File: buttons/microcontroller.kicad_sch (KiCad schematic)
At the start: 32 parts, among them J2 USB_C_Receptacle_USB2.0, J3 Conn_01x03, SW17 SW_SPST, SW18 SW_SPST, U2 RP2040, U3 ip4234cz6, U4 AMS1117-3.3, Y1 12MHz

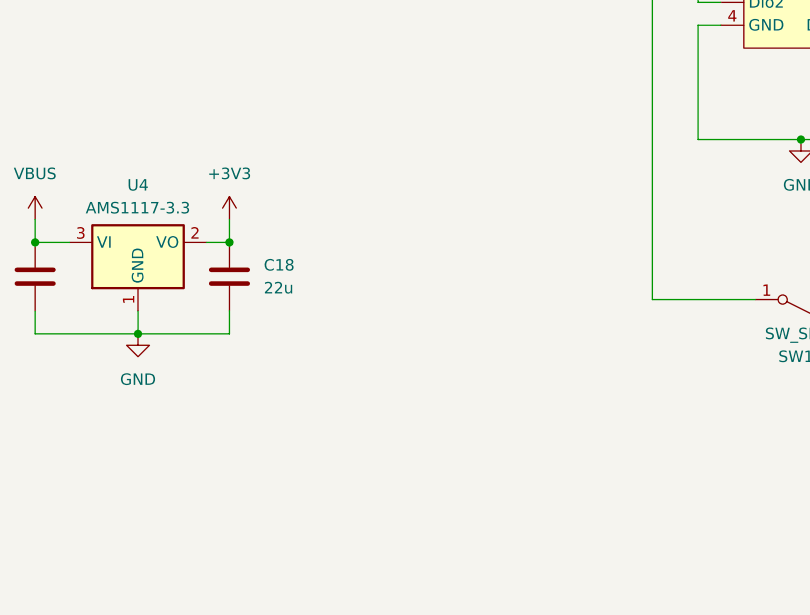
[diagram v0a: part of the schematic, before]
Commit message: Added power LED
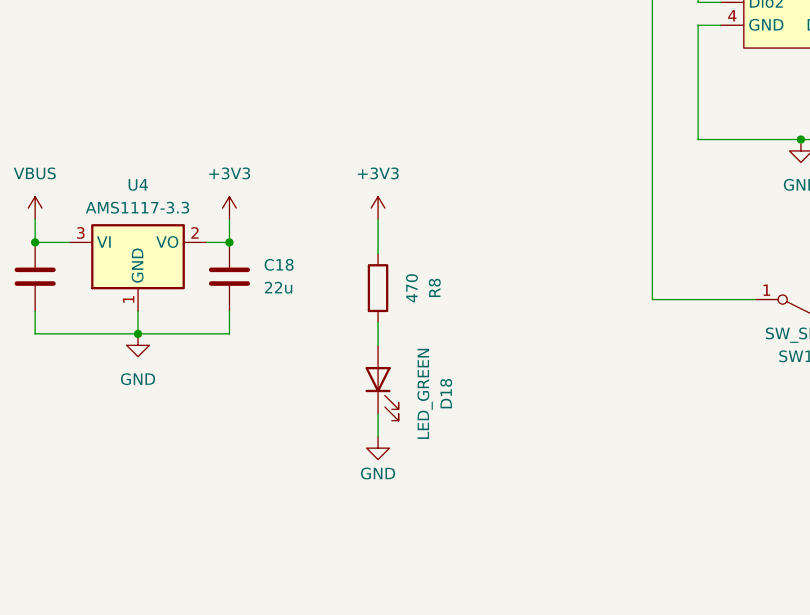
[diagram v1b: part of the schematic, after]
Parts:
- added D18: LED_GREEN, LED_SMD:LED_0603_1608Metric, symbol Device:LED
- added R8: 470, Resistor_SMD:R_0603_1608Metric, symbol Device:R
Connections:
- net +3V3: now also R8.1
- net GND: now also D18.1 (K)
- new net: D18.2 (A), R8.2
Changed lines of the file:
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@@
+    (stroke (width 0) (type default))
+  )
+  (wire (pts (xy 73.66 125.73) (xy 73.66 128.27))
     (stroke (width 0) (type default))
   )
@@
     (stroke (width 0) (type default))
   )
+  (wire (pts (xy 73.66 135.89) (xy 73.66 138.43))
+    (stroke (width 0) (type default))
+  )
   (wire (pts (xy 106.68 87.63) (xy 106.68 68.58))
     (stroke (width 0) (type default))
@@
   )
   (wire (pts (xy 142.24 77.47) (xy 173.99 77.47))
+    (stroke (width 0) (type default))
+  )
+  (wire (pts (xy 73.66 114.3) (xy 73.66 118.11))
     (stroke (width 0) (type default))
   )
@@
     )
   )
+  (symbol (lib_id "Device:LED") (at 73.66 132.08 90) (unit 1)
+    (in_bom yes) (on_board yes) (dnp no) (fields_autoplaced)
+    (property "Reference" "D18" (at 81.28 133.6675 0)
+      (effects (font (size 1.27 1.27)))
+    )
+    (property "Value" "LED_GREEN" (at 78.74 133.6675 0)
+      (effects (font (size 1.27 1.27)))
+    )
+    (property "Footprint" "LED_SMD:LED_0603_1608Metric" (at 73.66 132.08 0)
+      (effects (font (size 1.27 1.27)) hide)
+    )
+    (property "Datasheet" "~" (at 73.66 132.08 0)
+      (effects (font (size 1.27 1.27)) hide)
+    )
+    (pin "1")
+    (pin "2")
+    (instances
+      (project "buttons"
+        (path "/e63e39d7-6ac0-4ffd-8aa3-1841a4541b55/a606df9b-7133-4945-a21c-b987bfbff0f6"
+          (reference "D18") (unit 1)
+        )
+      )
+    )
+  )
   (symbol (lib_id "Device:C") (at 231.14 40.64 90) (unit 1)
     (in_bom yes) (on_board yes) (dnp no) (fields_autoplaced)
@@
         (path "/e63e39d7-6ac0-4ffd-8aa3-1841a4541b55/a606df9b-7133-4945-a21c-b987bfbff0f6"
           (reference "C30") (unit 1)
+        )
+      )
+    )
+  )
+  (symbol (lib_id "Device:R") (at 73.66 121.92 0) (unit 1)
+    (in_bom yes) (on_board yes) (dnp no) (fields_autoplaced)
+    (property "Reference" "R8" (at 80.01 121.92 90)
+      (effects (font (size 1.27 1.27)))
+    )
+    (property "Value" "470" (at 77.47 121.92 90)
+      (effects (font (size 1.27 1.27)))
+    )
+    (property "Footprint" "Resistor_SMD:R_0603_1608Metric" (at 71.882 121.92 90)
+      (effects (font (size 1.27 1.27)) hide)
+    )
+    (property "Datasheet" "~" (at 73.66 121.92 0)
+      (effects (font (size 1.27 1.27)) hide)
+    )
+    (pin "1")
+    (pin "2")
+    (instances
+      (project "buttons"
+        (path "/e63e39d7-6ac0-4ffd-8aa3-1841a4541b55/a606df9b-7133-4945-a21c-b987bfbff0f6"
+          (reference "R8") (unit 1)
         )
       )
@@
     )
   )
+  (symbol (lib_id "power:+3V3") (at 73.66 114.3 0) (unit 1)
+    (in_bom yes) (on_board yes) (dnp no) (fields_autoplaced)
+    (property "Reference" "#PWR022" (at 73.66 118.11 0)
+      (effects (font (size 1.27 1.27)) hide)
+    )
+    (property "Value" "+3V3" (at 73.66 109.22 0)
+      (effects (font (size 1.27 1.27)))
+    )
+    (property "Footprint" "" (at 73.66 114.3 0)
+      (effects (font (size 1.27 1.27)) hide)
+    )
+    (property "Datasheet" "" (at 73.66 114.3 0)
+      (effects (font (size 1.27 1.27)) hide)
+    )
+    (pin "1")
+    (instances
+      (project "buttons"
+        (path "/e63e39d7-6ac0-4ffd-8aa3-1841a4541b55/a606df9b-7133-4945-a21c-b987bfbff0f6"
+          (reference "#PWR022") (unit 1)
+        )
+      )
+    )
+  )
   (symbol (lib_id "power:GND") (at 152.4 53.34 0) (unit 1)
     (in_bom yes) (on_board yes) (dnp no) (fields_autoplaced)
@@
         )
       )
+    )
+  )
+  (symbol (lib_id "power:GND") (at 73.66 138.43 0) (unit 1)
+    (in_bom yes) (on_board yes) (dnp no) (fields_autoplaced)
+    (property "Reference" "#PWR021" (at 73.66 144.78 0)
+      (effects (font (size 1.27 1.27)) hide)
+    )
+    (property "Value" "GND" (at 73.66 142.5631 0)
+      (effects (font (size 1.27 1.27)))
+    )
+    (property "Footprint" "" (at 73.66 138.43 0)
+      (effects (font (size 1.27 1.27)) hide)
+    )
+    (property "Datasheet" "" (at 73.66 138.43 0)
+      (effects (font (size 1.27 1.27)) hide)
+    )
+    (pin "1")
+    (instances
+      (project "buttons"
+        (path "/e63e39d7-6ac0-4ffd-8aa3-1841a4541b55/a606df9b-7133-4945-a21c-b987bfbff0f6"
+          (reference "#PWR021") (unit 1)
+        )
+      )

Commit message: Picked components
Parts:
- C20, C21: DPN (none) -> 1292-1487-1-ND; MPN (none) -> 0603N150J500CT
- C22, C25: DPN CL10A225KP8NNNC -> 1276-1085-1-ND; MPN 1276-1085-1-ND -> CL10A225KP8NNNC
- C23, C24, C26, C27, C28, C29, C30, C31: DPN CL10B104KB8NNWC -> 1276-1935-1-ND; MPN 1276-1935-1-ND -> CL10B104KB8NNWC
- D17, D18: DPN (none) -> 3147-B1911PG--20D000514U1930CT-ND; MPN (none) -> B1911PG--20D000514U1930
- J2: DPN (none) -> 2073-USB4105-GF-ACT-ND; MPN (none) -> USB4105-GF-A
- J3: value Conn_01x03 -> DNP
- R1, R2: DPN (none) -> RMCF0603FT5K10CT-ND; MPN (none) -> RMCF0603FT5K10
- R3: value R -> 1k; DPN (none) -> RMCF0603FT1K00CT-ND; MPN (none) -> RMCF0603FT1K00
- R4: DPN (none) -> RMCF0603FT1R00CT-ND; MPN (none) -> RMCF0603FT1R00
- R5, R8: DPN (none) -> RMCF0603FT470RCT-ND; MPN (none) -> RMCF0603FT470R
- R6, R7: DPN (none) -> RMCF0603FT22R0CT-ND; MPN (none) -> RMCF0603FT22R0
- SW17, SW18: value SW_SPST -> DNP
- U2: DPN (none) -> 2648-SC0914(13)CT-ND; MPN (none) -> SC0914(13)
- U2: value ~ -> W25Q16JVUXIQ TR; DPN (none) -> 256-W25Q16JVUXIQTRCT-ND; MPN (none) -> W25Q16JVUXIQ TR
- U4: DPN (none) -> 4518-AMS1117-3.3CT-ND; MPN (none) -> AMS1117-3.3
- Y1: DPN (none) -> 2151-RH100-12.000-12-1010-X-TR-NS2CT-ND; MPN (none) -> RH100-12.000-12-1010-X-TR-NS2
